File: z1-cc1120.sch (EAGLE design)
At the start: 8 parts, among them X1 PN61729-S

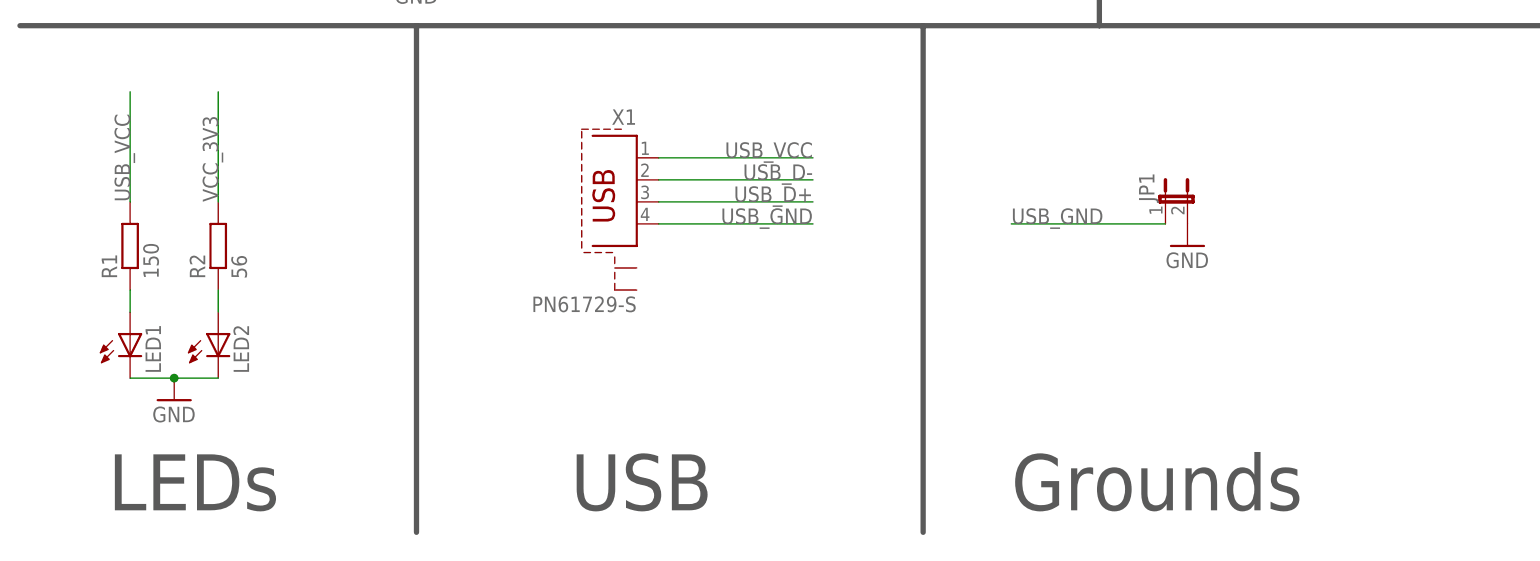
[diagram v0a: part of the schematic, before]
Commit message: Added silk screen info seperated usb_gnd & gnd added mounting holes
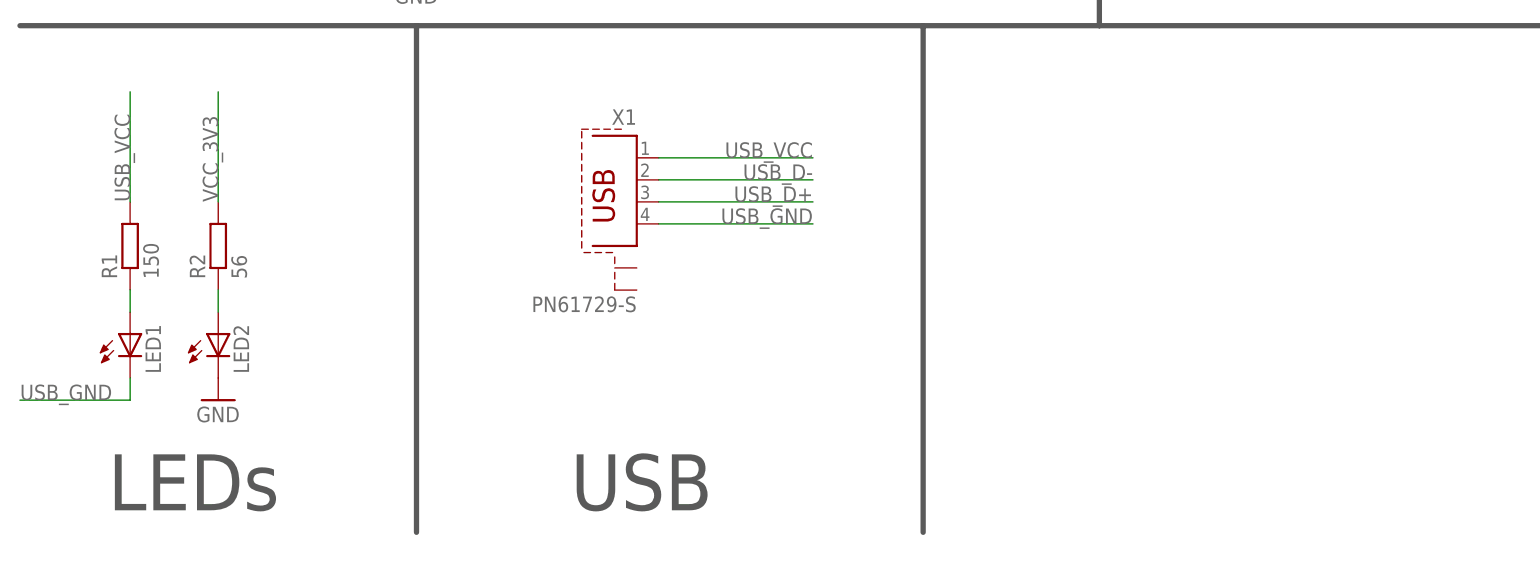
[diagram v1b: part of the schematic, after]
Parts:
- removed JP1: (no value), SparkFun-Passives:JUMPER-2SMD-NC
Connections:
- net GND: no longer JP1.2, LED1.C
- net USB_GND: now also LED1.C; no longer JP1.1
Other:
- note removed: "Grounds"
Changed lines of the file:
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@@
 <part name="R1" library="resistor" deviceset="R-EU_" device="R0805" value="150"/>
 <part name="GND1" library="supply1" deviceset="GND" device=""/>
-<part name="JP1" library="SparkFun-Passives" deviceset="JUMPER-2" device="SMD-NC"/>
-<part name="GND2" library="supply1" deviceset="GND" device=""/>
 <part name="GND3" library="supply1" deviceset="GND" device=""/>
 </parts>
@@
 <wire x1="109.22" y1="5.08" x2="109.22" y2="63.5" width="0.6096" layer="97"/>
 <wire x1="129.54" y1="175.26" x2="129.54" y2="63.5" width="0.6096" layer="97"/>
-<text x="119.38" y="7.62" size="6.4516" layer="97">Grounds</text>
 <text x="68.58" y="7.62" size="6.4516" layer="97">USB </text>
 <text x="15.24" y="7.62" size="6.4516" layer="97">LEDs</text>
@@
 <instance part="R1" gate="G$1" x="17.78" y="38.1" rot="R90"/>
 <instance part="X1" gate="G$1" x="76.2" y="43.18" rot="MR0"/>
-<instance part="GND1" gate="1" x="22.86" y="20.32"/>
-<instance part="JP1" gate="A" x="137.16" y="43.18"/>
-<instance part="GND2" gate="1" x="139.7" y="38.1"/>
+<instance part="GND1" gate="1" x="27.94" y="20.32"/>
 <instance part="GND3" gate="1" x="210.82" y="71.12"/>
 </instances>
@@
 </segment>
 <segment>
-<pinref part="LED1" gate="G$1" pin="C"/>
 <pinref part="LED2" gate="G$1" pin="C"/>
-<wire x1="17.78" y1="22.86" x2="22.86" y2="22.86" width="0.1524" layer="91"/>
 <pinref part="GND1" gate="1" pin="GND"/>
-<junction x="22.86" y="22.86"/>
-<wire x1="22.86" y1="22.86" x2="27.94" y2="22.86" width="0.1524" layer="91"/>
-</segment>
-<segment>
-<pinref part="JP1" gate="A" pin="2"/>
-<pinref part="GND2" gate="1" pin="GND"/>
 </segment>
 <segment>
@@
 </segment>
 <segment>
-<pinref part="JP1" gate="A" pin="1"/>
-<wire x1="137.16" y1="40.64" x2="119.38" y2="40.64" width="0.1524" layer="91"/>
-<label x="119.38" y="40.64" size="1.778" layer="95"/>
+<pinref part="LED1" gate="G$1" pin="C"/>
+<wire x1="17.78" y1="22.86" x2="17.78" y2="20.32" width="0.1524" layer="91"/>
+<wire x1="17.78" y1="20.32" x2="5.08" y2="20.32" width="0.1524" layer="91"/>
+<label x="5.08" y="20.32" size="1.778" layer="95"/>
 </segment>
 </net>

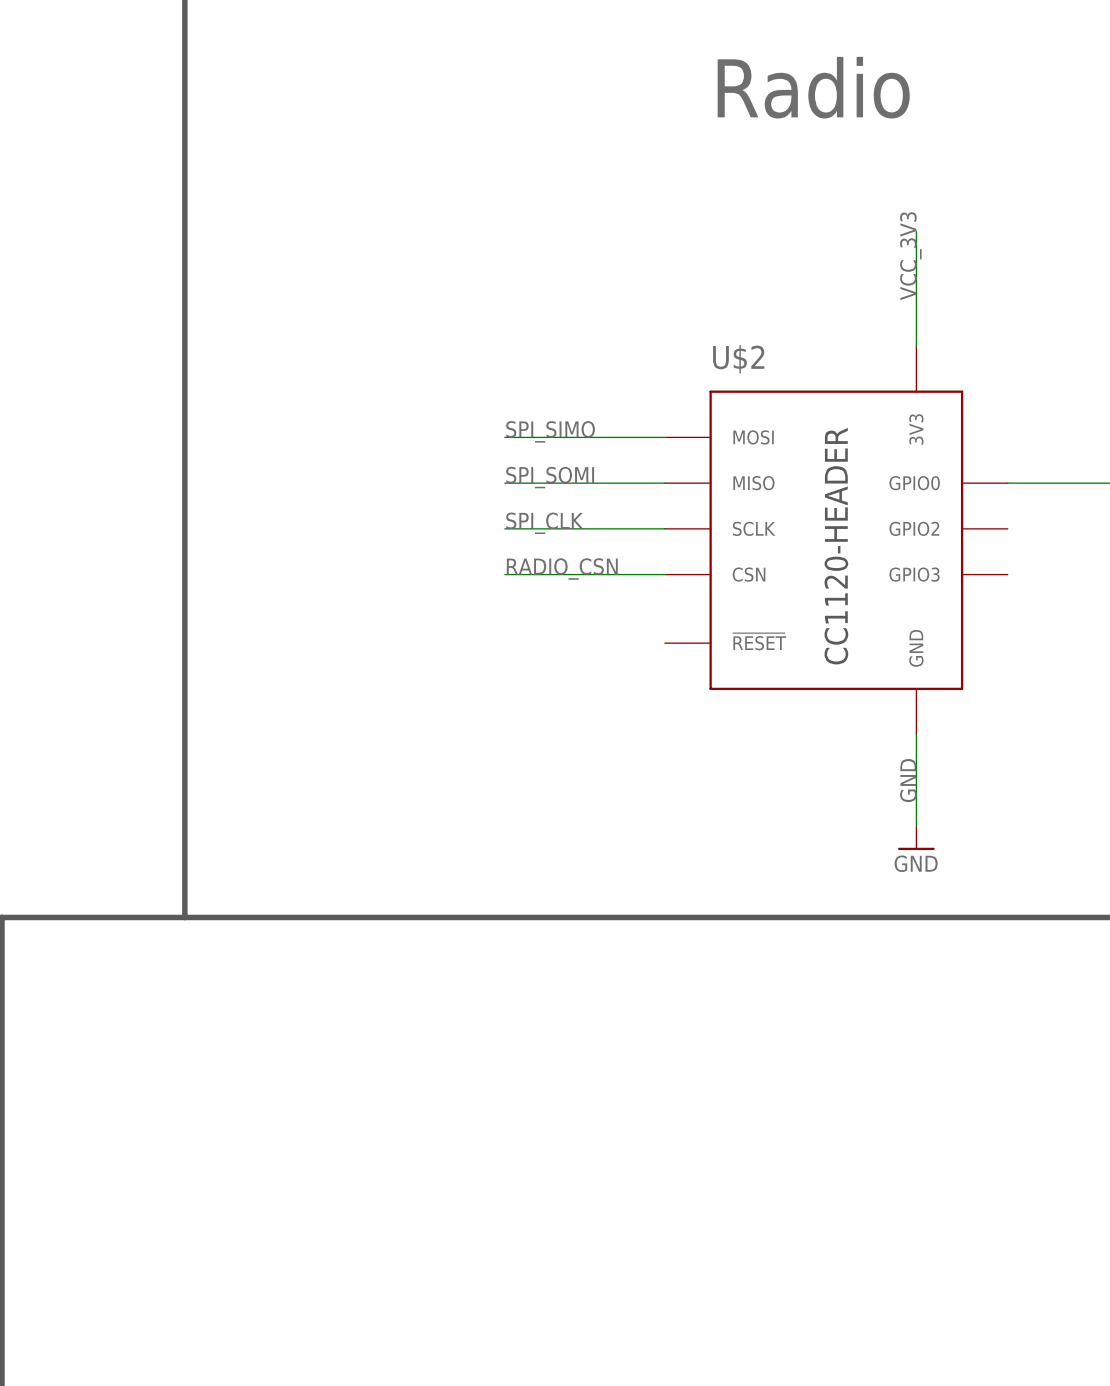
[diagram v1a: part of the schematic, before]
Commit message: Seperated radio gnd & vcc using inductor/cap network from z1 docs
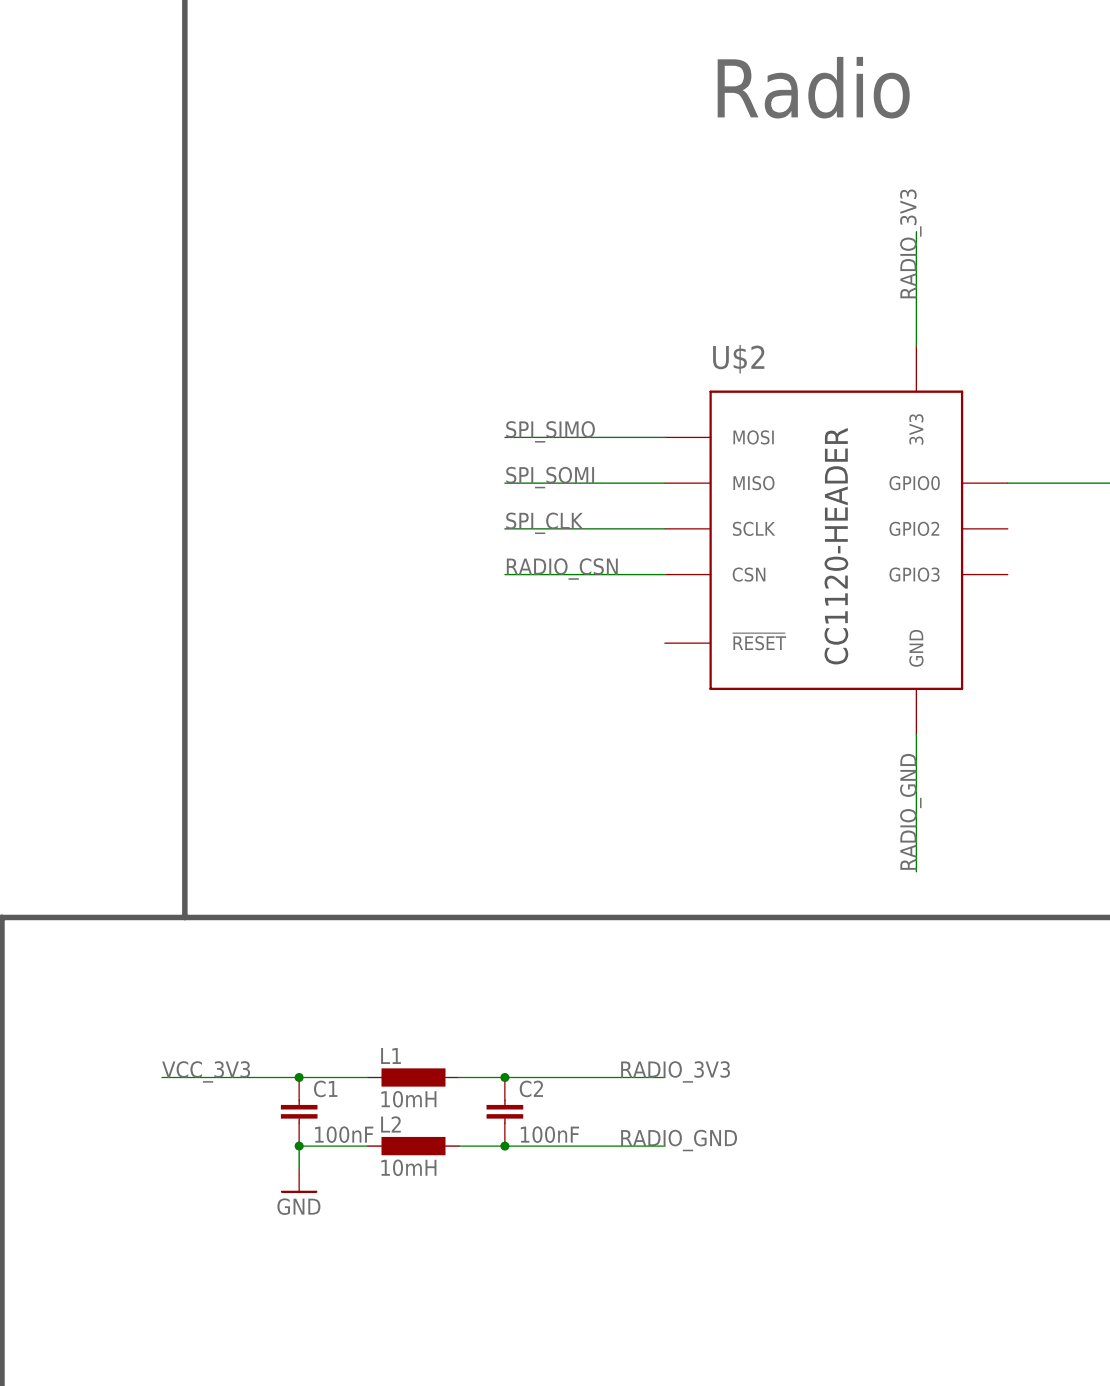
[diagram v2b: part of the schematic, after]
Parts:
- added C1, C2: 100nF, resistor:C-EUC0805
- added L1, L2: 10mH, resistor:L-EUL3230M
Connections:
- new net RADIO_3V3: C2.1, L1.1, U$2.3V3
- new net RADIO_GND: C2.2, L2.1, U$2.GND
- net GND: now also C1.2, L2.2; no longer U$2.GND
- net VCC_3V3: now also C1.1, L1.2; no longer U$2.3V3
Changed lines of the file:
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@@
 <part name="R1" library="resistor" deviceset="R-EU_" device="R0805" value="150"/>
 <part name="GND1" library="supply1" deviceset="GND" device=""/>
-<part name="GND3" library="supply1" deviceset="GND" device=""/>
+<part name="GND2" library="supply1" deviceset="GND" device=""/>
+<part name="C1" library="resistor" deviceset="C-EU" device="C0805" value="100nF"/>
+<part name="C2" library="resistor" deviceset="C-EU" device="C0805" value="100nF"/>
+<part name="L1" library="resistor" deviceset="L-EU" device="L3230M" value="10mH"/>
+<part name="L2" library="resistor" deviceset="L-EU" device="L3230M" value="10mH"/>
 </parts>
 <sheets>
@@
 <instance part="X1" gate="G$1" x="76.2" y="43.18" rot="MR0"/>
 <instance part="GND1" gate="1" x="27.94" y="20.32"/>
-<instance part="GND3" gate="1" x="210.82" y="71.12"/>
+<instance part="GND2" gate="1" x="142.24" y="33.02"/>
+<instance part="C1" gate="G$1" x="142.24" y="43.18"/>
+<instance part="C2" gate="G$1" x="165.1" y="43.18"/>
+<instance part="L1" gate="G$1" x="154.94" y="45.72" rot="R270"/>
+<instance part="L2" gate="G$1" x="154.94" y="38.1" rot="R270"/>
 </instances>
 <busses>
@@
 </segment>
 <segment>
-<pinref part="U$2" gate="G$1" pin="GND"/>
-<wire x1="210.82" y1="83.82" x2="210.82" y2="73.66" width="0.1524" layer="91"/>
-<label x="210.82" y="76.2" size="1.778" layer="95" rot="R90"/>
-<pinref part="GND3" gate="1" pin="GND"/>
+<pinref part="C1" gate="G$1" pin="2"/>
+<pinref part="GND2" gate="1" pin="GND"/>
+<wire x1="142.24" y1="38.1" x2="142.24" y2="35.56" width="0.1524" layer="91"/>
+<pinref part="L2" gate="G$1" pin="2"/>
+<wire x1="149.86" y1="38.1" x2="142.24" y2="38.1" width="0.1524" layer="91"/>
+<junction x="142.24" y="38.1"/>
 </segment>
 </net>
@@
 </segment>
 <segment>
-<pinref part="U$2" gate="G$1" pin="3V3"/>
-<wire x1="210.82" y1="127" x2="210.82" y2="139.7" width="0.1524" layer="91"/>
-<label x="210.82" y="132.08" size="1.778" layer="95" rot="R90"/>
+<pinref part="L1" gate="G$1" pin="2"/>
+<wire x1="149.86" y1="45.72" x2="142.24" y2="45.72" width="0.1524" layer="91"/>
+<label x="127" y="45.72" size="1.778" layer="95"/>
+<pinref part="C1" gate="G$1" pin="1"/>
+<junction x="142.24" y="45.72"/>
+<wire x1="142.24" y1="45.72" x2="127" y2="45.72" width="0.1524" layer="91"/>
 </segment>
 </net>
@@
 </segment>
 </net>
+<net name="RADIO_GND" class="0">
+<segment>
+<pinref part="U$2" gate="G$1" pin="GND"/>
+<wire x1="210.82" y1="83.82" x2="210.82" y2="68.58" width="0.1524" layer="91"/>
+<label x="210.82" y="68.58" size="1.778" layer="95" rot="R90"/>
+</segment>
+<segment>
+<pinref part="L2" gate="G$1" pin="1"/>
+<wire x1="160.02" y1="38.1" x2="165.1" y2="38.1" width="0.1524" layer="91"/>
+<label x="177.8" y="38.1" size="1.778" layer="95"/>
+<pinref part="C2" gate="G$1" pin="2"/>
+<junction x="165.1" y="38.1"/>
+<wire x1="165.1" y1="38.1" x2="182.88" y2="38.1" width="0.1524" layer="91"/>
+</segment>
+</net>
+<net name="RADIO_3V3" class="0">
+<segment>
+<pinref part="U$2" gate="G$1" pin="3V3"/>
+<wire x1="210.82" y1="127" x2="210.82" y2="139.7" width="0.1524" layer="91"/>
+<label x="210.82" y="132.08" size="1.778" layer="95" rot="R90"/>
+</segment>
+<segment>
+<pinref part="L1" gate="G$1" pin="1"/>
+<label x="177.8" y="45.72" size="1.778" layer="95"/>
+<wire x1="160.02" y1="45.72" x2="165.1" y2="45.72" width="0.1524" layer="91"/>
+<pinref part="C2" gate="G$1" pin="1"/>
+<junction x="165.1" y="45.72"/>
+<wire x1="165.1" y1="45.72" x2="182.88" y2="45.72" width="0.1524" layer="91"/>
+</segment>
+</net>

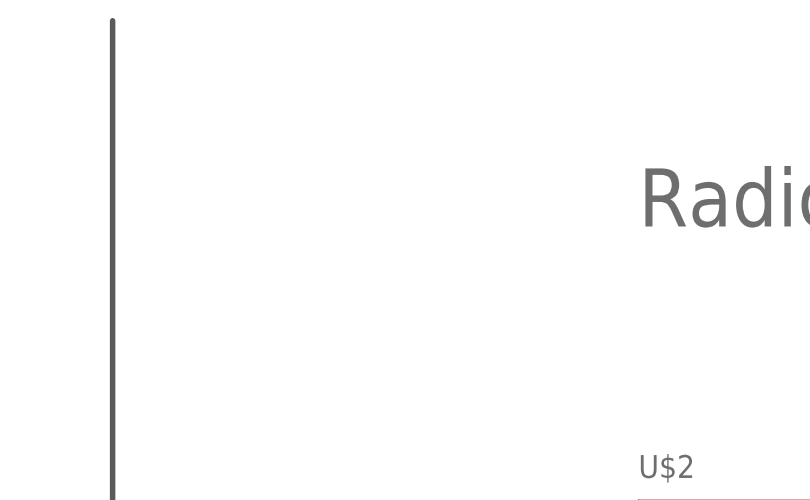
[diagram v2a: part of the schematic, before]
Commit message: added header to ease radio debug
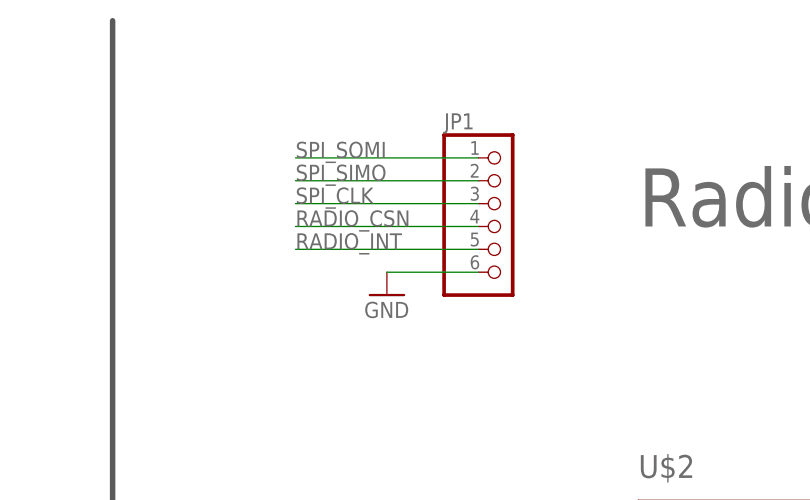
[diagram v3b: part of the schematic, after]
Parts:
- added JP1: (no value), pinhead:PINHD-1X6
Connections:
- net GND: now also JP1.6
- net RADIO_CSN: now also JP1.4
- net RADIO_INT: now also JP1.5
- net SPI_CLK: now also JP1.3
- net SPI_SIMO: now also JP1.2
- net SPI_SOMI: now also JP1.1
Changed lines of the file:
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@@
 <part name="L1" library="resistor" deviceset="L-EU" device="L3230M" value="10mH"/>
 <part name="L2" library="resistor" deviceset="L-EU" device="L3230M" value="10mH"/>
+<part name="JP1" library="pinhead" deviceset="PINHD-1X6" device=""/>
+<part name="GND3" library="supply1" deviceset="GND" device=""/>
 </parts>
 <sheets>
@@
 <instance part="L1" gate="G$1" x="154.94" y="45.72" rot="R270"/>
 <instance part="L2" gate="G$1" x="154.94" y="38.1" rot="R270"/>
+<instance part="JP1" gate="A" x="172.72" y="152.4"/>
+<instance part="GND3" gate="1" x="160.02" y="144.78"/>
 </instances>
 <busses>
@@
 <junction x="142.24" y="38.1"/>
 </segment>
+<segment>
+<pinref part="GND3" gate="1" pin="GND"/>
+<pinref part="JP1" gate="A" pin="6"/>
+<wire x1="170.18" y1="147.32" x2="160.02" y2="147.32" width="0.1524" layer="91"/>
+</segment>
 </net>
 <net name="VCC_3V3" class="0">
@@
 <label x="165.1" y="106.68" size="1.778" layer="95"/>
 </segment>
+<segment>
+<pinref part="JP1" gate="A" pin="3"/>
+<wire x1="170.18" y1="154.94" x2="149.86" y2="154.94" width="0.1524" layer="91"/>
+<label x="149.86" y="154.94" size="1.778" layer="95"/>
+</segment>
 </net>
 <net name="SPI_SIMO" class="0">
@@
 <label x="165.1" y="116.84" size="1.778" layer="95"/>
 </segment>
+<segment>
+<pinref part="JP1" gate="A" pin="2"/>
+<wire x1="170.18" y1="157.48" x2="149.86" y2="157.48" width="0.1524" layer="91"/>
+<label x="149.86" y="157.48" size="1.778" layer="95"/>
+</segment>
 </net>
 <net name="SPI_SOMI" class="0">
@@
 <label x="165.1" y="111.76" size="1.778" layer="95"/>
 </segment>
+<segment>
+<pinref part="JP1" gate="A" pin="1"/>
+<wire x1="170.18" y1="160.02" x2="149.86" y2="160.02" width="0.1524" layer="91"/>
+<label x="149.86" y="160.02" size="1.778" layer="95"/>
+</segment>
 </net>
 <net name="RADIO_CSN" class="0">
@@
 <wire x1="30.48" y1="99.06" x2="12.7" y2="99.06" width="0.1524" layer="91"/>
 <label x="12.7" y="99.06" size="1.778" layer="95"/>
+</segment>
+<segment>
+<pinref part="JP1" gate="A" pin="4"/>
+<wire x1="170.18" y1="152.4" x2="149.86" y2="152.4" width="0.1524" layer="91"/>
+<label x="149.86" y="152.4" size="1.778" layer="95"/>
 </segment>
 </net>
@@
 <label x="236.22" y="111.76" size="1.778" layer="95"/>
 </segment>
-</net>
+<segment>
+<pinref part="JP1" gate="A" pin="5"/>
+<wire x1="170.18" y1="149.86" x2="149.86" y2="149.86" width="0.1524" layer="91"/>
+<label x="149.86" y="149.86" size="1.778" layer="95"/>
+</segment>
+</net>
